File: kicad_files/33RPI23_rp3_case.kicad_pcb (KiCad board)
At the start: 2 copper layers, 56 x 85 mm, 110 parts, among them CN1 locked, J1 VGA, J10 AudioJack4, J11 USB_B_Micro, J12 Mini-DIN-6, J13 Mini-DIN-6, J14 Conn_01x07, J15 Conn_01x01_Female, J16 USB, J17 Conn_01x02_Female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

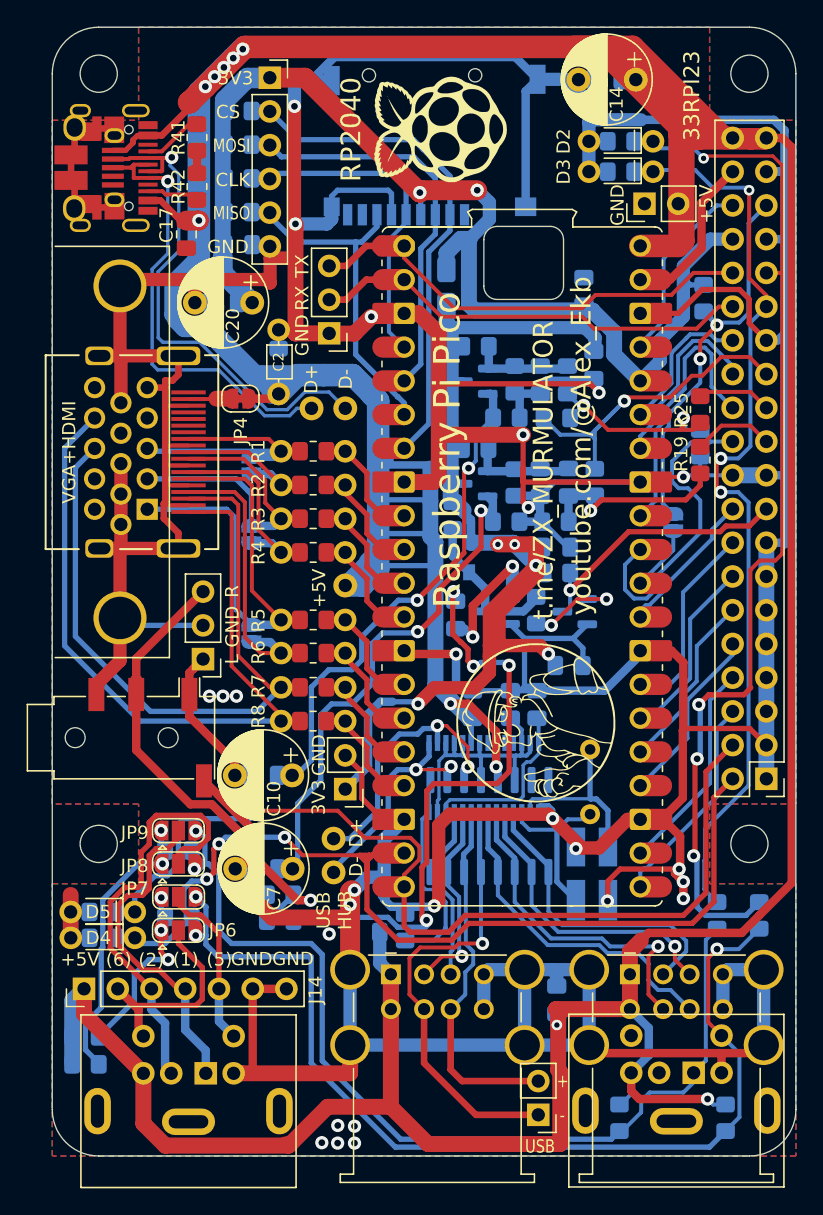
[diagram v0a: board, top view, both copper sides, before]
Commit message: .
Power Led
USB IN d+ d- position
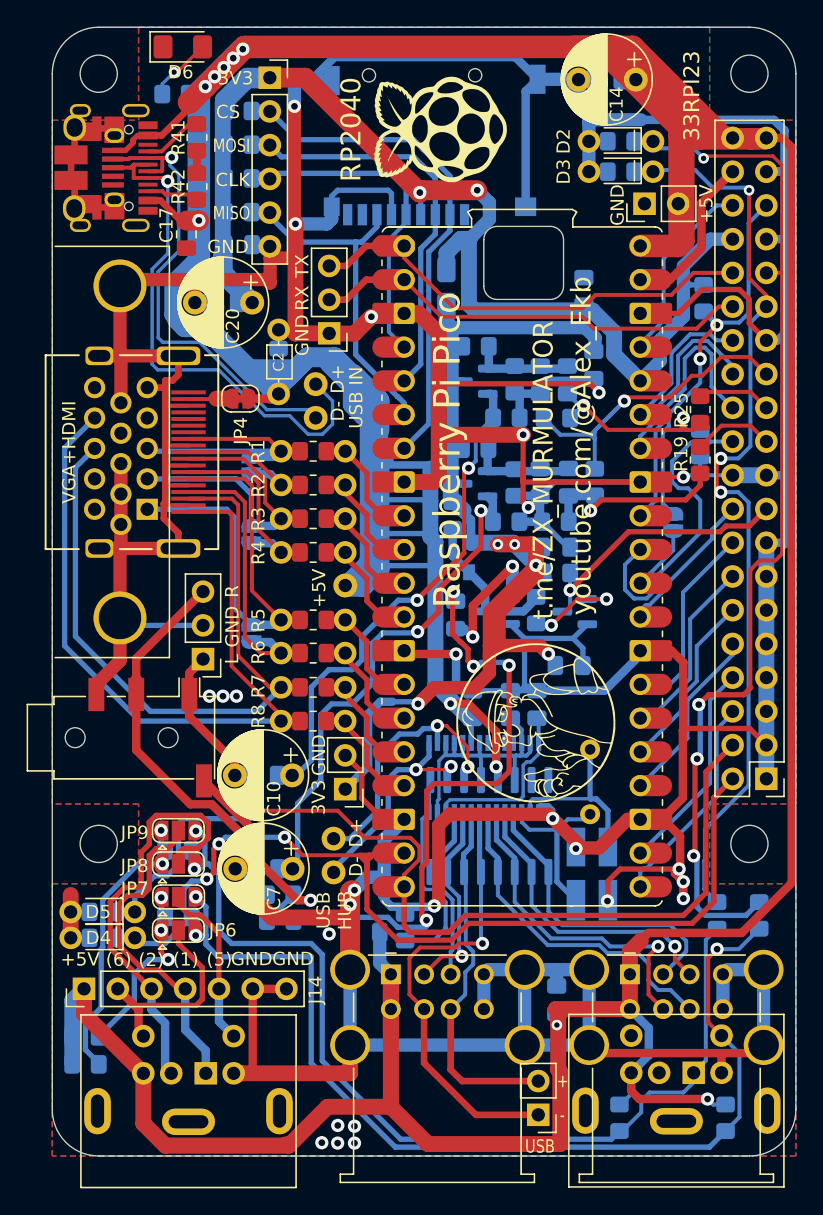
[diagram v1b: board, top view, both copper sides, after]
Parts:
- added D6: LED_Small, LED_SMD:LED_1206_3216Metric_Pad1.42x1.75mm_HandSolder, F.Cu at (35.3, 30.5)
- added R43: 300, Resistor_SMD:R_0805_2012Metric_Pad1.20x1.40mm_HandSolder, B.Cu at (34.8, 34.0)
- moved J18 1.85 mm to (45.3, 55.9), turned to 0 degrees
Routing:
- net /+5V: track 558.9 -> 588.2 mm
- net /D+: track 34.1 -> 39.9 mm
- net Net-(D6-Pad2): track 0.00 -> 4.95 mm, vias 0 -> 1
- net /D-: track 38.7 -> 35.7 mm
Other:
- board text added: "USB IN"
